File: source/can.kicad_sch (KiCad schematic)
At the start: 5 parts

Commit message: Add files via upload
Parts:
- C3: renamed from C?; value 1nF -> 1n
- gave numbers to parts that had none: 4
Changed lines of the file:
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@@
 (kicad_sch (version 20211123) (generator eeschema)
   (paper "A4")
+  (junction (at 163.83 83.82) (diameter 0) (color 0 0 0 0)
+  )
   (junction (at 132.08 85.09) (diameter 0) (color 0 0 0 0)
   )
@@
     (stroke (width 0) (type default) (color 0 0 0 0))
   )
+  (wire (pts (xy 163.83 83.82) (xy 163.83 88.9))
+    (stroke (width 0) (type default) (color 0 0 0 0))
+  )
   (wire (pts (xy 171.45 77.47) (xy 163.83 77.47))
     (stroke (width 0) (type default) (color 0 0 0 0))
@@
     (stroke (width 0) (type default) (color 0 0 0 0))
   )
+  (wire (pts (xy 162.56 83.82) (xy 163.83 83.82))
+    (stroke (width 0) (type default) (color 0 0 0 0))
+  )
   (wire (pts (xy 124.46 104.14) (xy 124.46 111.76))
     (stroke (width 0) (type default) (color 0 0 0 0))
   )
-  (wire (pts (xy 163.83 77.47) (xy 163.83 88.9))
+  (wire (pts (xy 163.83 77.47) (xy 163.83 83.82))
     (stroke (width 0) (type default) (color 0 0 0 0))
   )
@@
   (symbol (lib_id "BLDC_4-rescue:+5V") (at 163.83 73.66 0) (unit 1)
     (in_bom yes) (on_board yes)
-    (property "Reference" "#PWR?" (id 0) (at 163.83 71.374 0)
+    (property "Reference" "#PWR0119" (id 0) (at 163.83 71.374 0)
       (effects (font (size 0.508 0.508)) hide)
     )
@@
     (pin "1")
   )
+  (symbol (lib_id "power:PWR_FLAG") (at 162.56 83.82 90) (unit 1)
+    (in_bom yes) (on_board yes) (fields_autoplaced)
+    (property "Reference" "#FLG0102" (id 0) (at 160.655 83.82 0)
+      (effects (font (size 1.27 1.27)) hide)
+    )
+    (property "Value" "PWR_FLAG" (id 1) (at 158.75 83.8199 90)
+      (effects (font (size 1.27 1.27)) (justify left))
+    )
+    (property "Footprint" "" (id 2) (at 162.56 83.82 0)
+      (effects (font (size 1.27 1.27)) hide)
+    )
+    (property "Datasheet" "~" (id 3) (at 162.56 83.82 0)
+      (effects (font (size 1.27 1.27)) hide)
+    )
+    (pin "1")
+  )
   (symbol (lib_id "BLDC_4-rescue:MCP2551-I_SN-RESCUE-BLDC_4") (at 163.83 99.06 0) (mirror y) (unit 1)
     (in_bom yes) (on_board yes)
-    (property "Reference" "U?" (id 0) (at 170.18 91.44 0)
+    (property "Reference" "U1" (id 0) (at 170.18 91.44 0)
       (effects (font (size 1.016 1.016)))
     )
@@
   (symbol (lib_id "BLDC_4-rescue:C-RESCUE-BLDC_4") (at 171.45 82.55 0) (unit 1)
     (in_bom yes) (on_board yes)
-    (property "Reference" "C?" (id 0) (at 171.45 80.01 0)
+    (property "Reference" "C4" (id 0) (at 171.45 80.01 0)
       (effects (font (size 1.016 1.016)) (justify left))
     )
@@
   (symbol (lib_id "BLDC_4-rescue:C-RESCUE-BLDC_4") (at 138.43 99.06 90) (unit 1)
     (in_bom yes) (on_board yes)
-    (property "Reference" "C?" (id 0) (at 135.89 97.79 90)
-      (effects (font (size 1.016 1.016)) (justify left))
-    )
-    (property "Value" "1nF" (id 1) (at 143.51 97.79 90)
+    (property "Reference" "C3" (id 0) (at 135.89 97.79 90)
+      (effects (font (size 1.016 1.016)) (justify left))
+    )
+    (property "Value" "1n" (id 1) (at 143.51 97.79 90)
       (effects (font (size 1.016 1.016)) (justify left))
     )
@@
   (symbol (lib_id "power:VCC") (at 184.15 99.06 0) (unit 1)
     (in_bom yes) (on_board yes) (fields_autoplaced)
-    (property "Reference" "#PWR?" (id 0) (at 184.15 102.87 0)
+    (property "Reference" "#PWR0124" (id 0) (at 184.15 102.87 0)
       (effects (font (size 1.27 1.27)) hide)
     )
@@
   (symbol (lib_id "BLDC_4-rescue:R-RESCUE-BLDC_4") (at 132.08 105.41 0) (unit 1)
     (in_bom yes) (on_board yes)
-    (property "Reference" "R?" (id 0) (at 134.112 105.41 90)
+    (property "Reference" "R13" (id 0) (at 134.112 105.41 90)
       (effects (font (size 1.016 1.016)))
     )
@@
   (symbol (lib_id "BLDC_4-rescue:GND-RESCUE-BLDC_4") (at 144.78 99.06 90) (unit 1)
     (in_bom yes) (on_board yes)
-    (property "Reference" "#PWR?" (id 0) (at 144.78 99.06 0)
+    (property "Reference" "#PWR0123" (id 0) (at 144.78 99.06 0)
       (effects (font (size 0.762 0.762)) hide)
     )
@@
   (symbol (lib_id "BLDC_4-rescue:R-RESCUE-BLDC_4") (at 132.08 91.44 0) (unit 1)
     (in_bom yes) (on_board yes)
-    (property "Reference" "R?" (id 0) (at 134.112 91.44 90)
+    (property "Reference" "R12" (id 0) (at 134.112 91.44 90)
       (effects (font (size 1.016 1.016)))
     )
@@
   (symbol (lib_id "power:GND") (at 163.83 113.03 0) (unit 1)
     (in_bom yes) (on_board yes)
-    (property "Reference" "#PWR?" (id 0) (at 163.83 119.38 0)
+    (property "Reference" "#PWR0121" (id 0) (at 163.83 119.38 0)
       (effects (font (size 1.27 1.27)) hide)
     )
@@
   (symbol (lib_id "BLDC_4-rescue:GND-RESCUE-BLDC_4") (at 171.45 87.63 0) (unit 1)
     (in_bom yes) (on_board yes)
-    (property "Reference" "#PWR?" (id 0) (at 171.45 87.63 0)
+    (property "Reference" "#PWR0120" (id 0) (at 171.45 87.63 0)
       (effects (font (size 0.762 0.762)) hide)
     )
@@
   (symbol (lib_id "power:GND") (at 177.8 106.68 0) (unit 1)
     (in_bom yes) (on_board yes)
-    (property "Reference" "#PWR?" (id 0) (at 177.8 113.03 0)
-      (effects (font (size 1.27 1.27)) hide)
-    )
+    (property "Reference" "#PWR0122" (id 0) (at 177.8 113.03 0)
+      (effects (font (size 1.27 1.27)) hide)
+    )

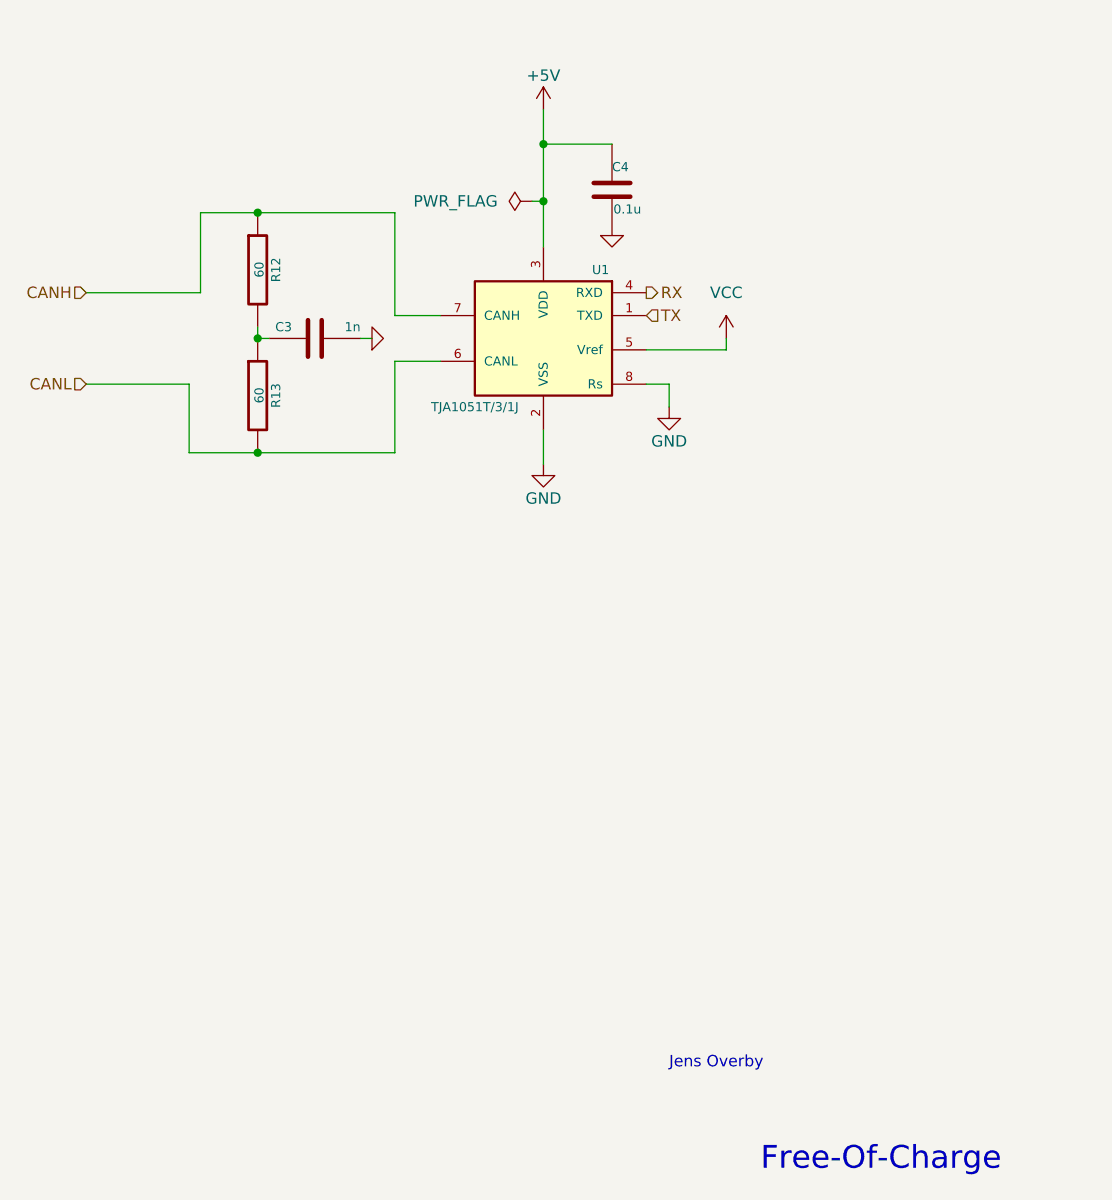
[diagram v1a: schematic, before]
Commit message: Changes suggested by mxlemming, Elwin and hackey on Discord
New power supplies and using other op-amps for current sense
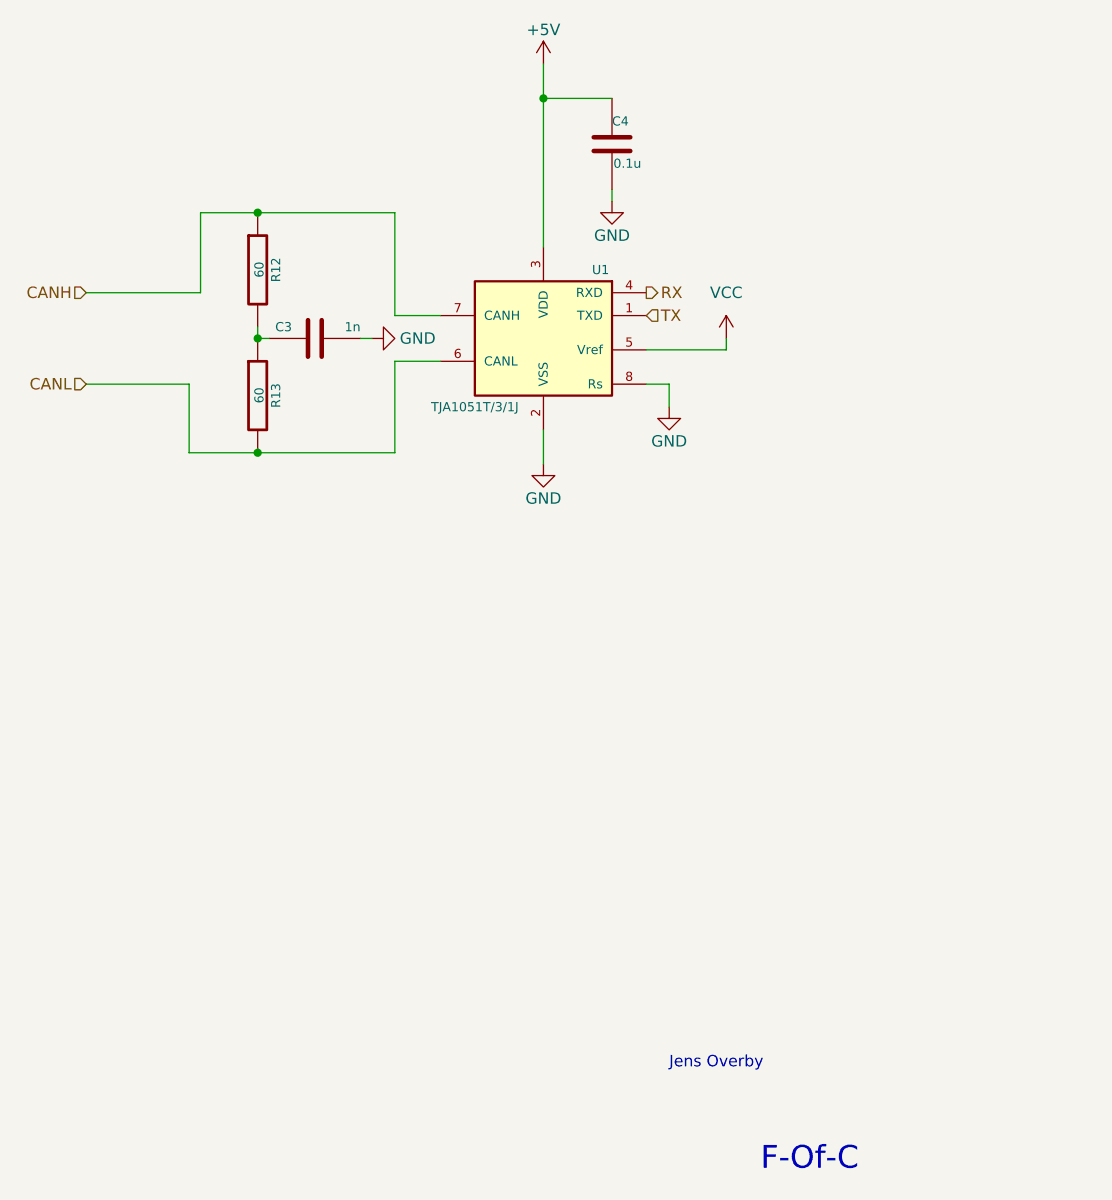
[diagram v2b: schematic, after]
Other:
- note added: "F-Of-C"
- note removed: "Free-Of-Charge"
- moved on the sheet: C4
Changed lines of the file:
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@@
 (kicad_sch (version 20211123) (generator eeschema)
   (paper "A4")
-  (junction (at 163.83 83.82) (diameter 0) (color 0 0 0 0)
-  )
   (junction (at 132.08 85.09) (diameter 0) (color 0 0 0 0)
   )
   (junction (at 132.08 111.76) (diameter 0) (color 0 0 0 0)
   )
-  (junction (at 163.83 77.47) (diameter 0) (color 0 0 0 0)
+  (junction (at 163.83 72.39) (diameter 0) (color 0 0 0 0)
   )
   (junction (at 132.08 99.06) (diameter 0) (color 0 0 0 0)
@@
     (stroke (width 0) (type default) (color 0 0 0 0))
   )
-  (wire (pts (xy 163.83 73.66) (xy 163.83 77.47))
+  (wire (pts (xy 163.83 68.58) (xy 163.83 72.39))
     (stroke (width 0) (type default) (color 0 0 0 0))
   )
@@
     (stroke (width 0) (type default) (color 0 0 0 0))
   )
+  (wire (pts (xy 171.45 82.55) (xy 171.45 83.82))
+    (stroke (width 0) (type default) (color 0 0 0 0))
+  )
   (wire (pts (xy 152.4 96.52) (xy 147.32 96.52))
     (stroke (width 0) (type default) (color 0 0 0 0))
   )
-  (wire (pts (xy 163.83 83.82) (xy 163.83 88.9))
-    (stroke (width 0) (type default) (color 0 0 0 0))
-  )
-  (wire (pts (xy 171.45 77.47) (xy 163.83 77.47))
+  (wire (pts (xy 171.45 72.39) (xy 163.83 72.39))
     (stroke (width 0) (type default) (color 0 0 0 0))
   )
@@
     (stroke (width 0) (type default) (color 0 0 0 0))
   )
-  (wire (pts (xy 162.56 83.82) (xy 163.83 83.82))
-    (stroke (width 0) (type default) (color 0 0 0 0))
-  )
   (wire (pts (xy 124.46 104.14) (xy 124.46 111.76))
     (stroke (width 0) (type default) (color 0 0 0 0))
   )
-  (wire (pts (xy 163.83 77.47) (xy 163.83 83.82))
+  (wire (pts (xy 163.83 72.39) (xy 163.83 88.9))
     (stroke (width 0) (type default) (color 0 0 0 0))
   )
@@
     (stroke (width 0) (type default) (color 0 0 0 0))
   )
-  (text "Free-Of-Charge" (at 187.96 191.77 0)
+  (text "F-Of-C" (at 187.96 191.77 0)
     (effects (font (size 2.54 2.54)) (justify left bottom))
   )
@@
     (effects (font (size 1.27 1.27)) (justify left))
   )
-  (symbol (lib_id "BLDC_4-rescue:+5V") (at 163.83 73.66 0) (unit 1)
-    (in_bom yes) (on_board yes)
-    (property "Reference" "#PWR0119" (id 0) (at 163.83 71.374 0)
+  (symbol (lib_id "BLDC_4-rescue:+5V") (at 163.83 68.58 0) (unit 1)
+    (in_bom yes) (on_board yes)
+    (property "Reference" "#PWR0119" (id 0) (at 163.83 66.294 0)
       (effects (font (size 0.508 0.508)) hide)
     )
-    (property "Value" "+5V" (id 1) (at 163.83 69.85 0))
-    (property "Footprint" "" (id 2) (at 163.83 73.66 0)
+    (property "Value" "+5V" (id 1) (at 163.83 64.77 0))
+    (property "Footprint" "" (id 2) (at 163.83 68.58 0)
       (effects (font (size 1.524 1.524)) hide)
     )
-    (property "Datasheet" "" (id 3) (at 163.83 73.66 0)
+    (property "Datasheet" "" (id 3) (at 163.83 68.58 0)
       (effects (font (size 1.524 1.524)) hide)
     )
     (pin "1")
   )
-  (symbol (lib_id "power:PWR_FLAG") (at 162.56 83.82 90) (unit 1)
-    (in_bom yes) (on_board yes) (fields_autoplaced)
-    (property "Reference" "#FLG0102" (id 0) (at 160.655 83.82 0)
-      (effects (font (size 1.27 1.27)) hide)
-    )
-    (property "Value" "PWR_FLAG" (id 1) (at 158.75 83.8199 90)
-      (effects (font (size 1.27 1.27)) (justify left))
-    )
-    (property "Footprint" "" (id 2) (at 162.56 83.82 0)
-      (effects (font (size 1.27 1.27)) hide)
-    )
-    (property "Datasheet" "~" (id 3) (at 162.56 83.82 0)
+  (symbol (lib_id "power:GND") (at 144.78 99.06 90) (unit 1)
+    (in_bom yes) (on_board yes)
+    (property "Reference" "#PWR0123" (id 0) (at 151.13 99.06 0)
+      (effects (font (size 1.27 1.27)) hide)
+    )
+    (property "Value" "GND" (id 1) (at 149.86 99.06 90))
+    (property "Footprint" "" (id 2) (at 144.78 99.06 0)
+      (effects (font (size 1.27 1.27)) hide)
+    )
+    (property "Datasheet" "" (id 3) (at 144.78 99.06 0)
       (effects (font (size 1.27 1.27)) hide)
     )
@@
     (pin "8")
   )
-  (symbol (lib_id "BLDC_4-rescue:C-RESCUE-BLDC_4") (at 171.45 82.55 0) (unit 1)
-    (in_bom yes) (on_board yes)
-    (property "Reference" "C4" (id 0) (at 171.45 80.01 0)
-      (effects (font (size 1.016 1.016)) (justify left))
-    )
-    (property "Value" "0.1u" (id 1) (at 171.6024 84.709 0)
-      (effects (font (size 1.016 1.016)) (justify left))
-    )
-    (property "Footprint" "Capacitor_SMD:C_0603_1608Metric" (id 2) (at 172.4152 86.36 0)
-      (effects (font (size 0.762 0.762)) hide)
-    )
-    (property "Datasheet" "" (id 3) (at 171.45 82.55 0)
+  (symbol (lib_id "BLDC_4-rescue:C-RESCUE-BLDC_4") (at 171.45 77.47 0) (unit 1)
+    (in_bom yes) (on_board yes)
+    (property "Reference" "C4" (id 0) (at 171.45 74.93 0)
+      (effects (font (size 1.016 1.016)) (justify left))
+    )
+    (property "Value" "0.1u" (id 1) (at 171.6024 79.629 0)
+      (effects (font (size 1.016 1.016)) (justify left))
+    )
+    (property "Footprint" "Capacitor_SMD:C_0603_1608Metric" (id 2) (at 172.4152 81.28 0)
+      (effects (font (size 0.762 0.762)) hide)
+    )
+    (property "Datasheet" "" (id 3) (at 171.45 77.47 0)
       (effects (font (size 1.524 1.524)))
     )
@@
     (pin "1")
   )
+  (symbol (lib_id "power:GND") (at 171.45 83.82 0) (unit 1)
+    (in_bom yes) (on_board yes)
+    (property "Reference" "#PWR0120" (id 0) (at 171.45 90.17 0)
+      (effects (font (size 1.27 1.27)) hide)
+    )
+    (property "Value" "GND" (id 1) (at 171.45 87.63 0))
+    (property "Footprint" "" (id 2) (at 171.45 83.82 0)
+      (effects (font (size 1.27 1.27)) hide)
+    )
+    (property "Datasheet" "" (id 3) (at 171.45 83.82 0)
+      (effects (font (size 1.27 1.27)) hide)
+    )
+    (pin "1")
+  )
   (symbol (lib_id "BLDC_4-rescue:R-RESCUE-BLDC_4") (at 132.08 105.41 0) (unit 1)
     (in_bom yes) (on_board yes)
@@
     (pin "2")
   )
-  (symbol (lib_id "BLDC_4-rescue:GND-RESCUE-BLDC_4") (at 144.78 99.06 90) (unit 1)
-    (in_bom yes) (on_board yes)
-    (property "Reference" "#PWR0123" (id 0) (at 144.78 99.06 0)
-      (effects (font (size 0.762 0.762)) hide)
-    )
-    (property "Value" "GND" (id 1) (at 146.558 99.06 0)
-      (effects (font (size 0.762 0.762)) hide)
-    )
-    (property "Footprint" "" (id 2) (at 144.78 99.06 0)
-      (effects (font (size 1.524 1.524)))
-    )
-    (property "Datasheet" "" (id 3) (at 144.78 99.06 0)
-      (effects (font (size 1.524 1.524)))
-    )
-    (pin "1")
-  )
   (symbol (lib_id "BLDC_4-rescue:R-RESCUE-BLDC_4") (at 132.08 91.44 0) (unit 1)
     (in_bom yes) (on_board yes)
@@
     )
     (pin "1")
-  )
-  (symbol (lib_id "BLDC_4-rescue:GND-RESCUE-BLDC_4") (at 171.45 87.63 0) (unit 1)
-    (in_bom yes) (on_board yes)
-    (property "Reference" "#PWR0120" (id 0) (at 171.45 87.63 0)
-      (effects (font (size 0.762 0.762)) hide)
-    )
-    (property "Value" "GND" (id 1) (at 171.45 89.408 0)
-      (effects (font (size 0.762 0.762)) hide)
-    )
-    (property "Footprint" "" (id 2) (at 171.45 87.63 0)
-      (effects (font (size 1.524 1.524)))
-    )
-    (property "Datasheet" "" (id 3) (at 171.45 87.63 0)
-      (effects (font (size 1.524 1.524)))
-    )
-    (pin "1")
